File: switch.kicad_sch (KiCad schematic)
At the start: 3 parts

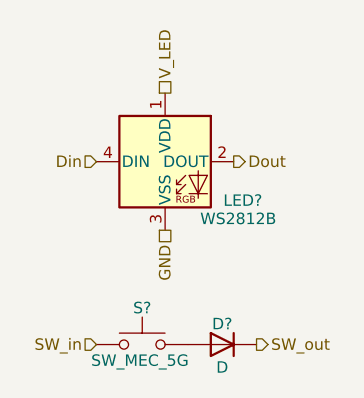
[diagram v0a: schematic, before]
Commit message: Replace LEDs with reverse mount variant
Previous LEDs collided with switch
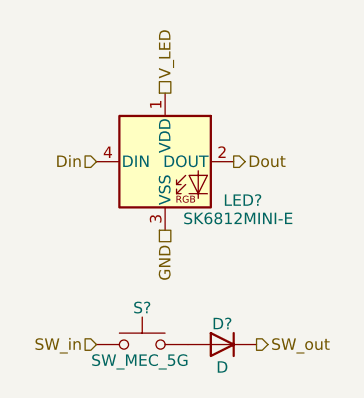
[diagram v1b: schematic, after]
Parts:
- LED?: value WS2812B -> SK6812MINI-E; footprint footprints:WS2812B -> footprints:SK6812MINI-E_RVRSMOUNT
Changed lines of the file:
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@@
 			)
 		)
-		(property "Value" "WS2812B"
+		(property "Value" "SK6812MINI-E"
 			(at 156.718 49.53 0)
 			(effects
@@
 			)
 		)
-		(property "Footprint" "footprints:WS2812B"
+		(property "Footprint" "footprints:SK6812MINI-E_RVRSMOUNT"
 			(at 149.86 50.8 0)
 			(effects
@@
 			)
 		)
-		(property "Datasheet" "https://cdn-shop.adafruit.com/datasheets/WS2812B.pdf"
+		(property "Datasheet" ""
 			(at 151.13 52.705 0)
 			(effects
@@
 		)
 	)
+	(sheet_instances
+		(path "/"
+			(page "1")
+		)
+	)
